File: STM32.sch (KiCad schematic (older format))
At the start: 35 parts, among them U1 STM32H753IIKx, U4 FM25V02A-GTR, U9 USB3300-EZK-TR, Y1 16MHz, Y2 32.768, Y3 24MHz

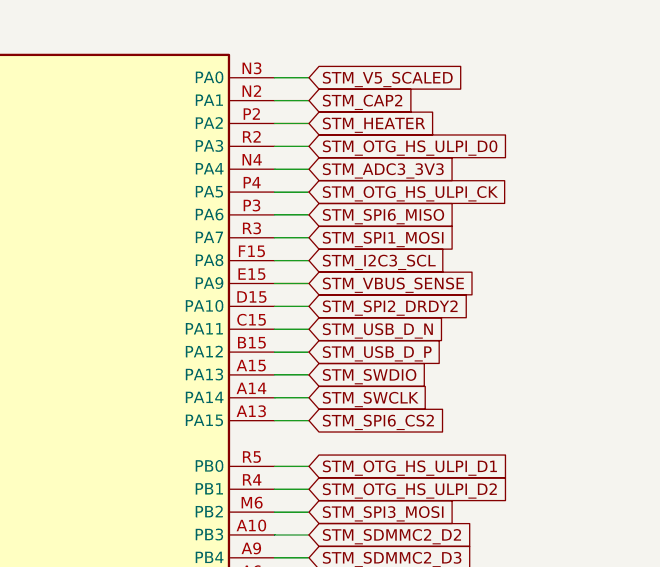
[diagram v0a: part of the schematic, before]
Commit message: start adding usb-c
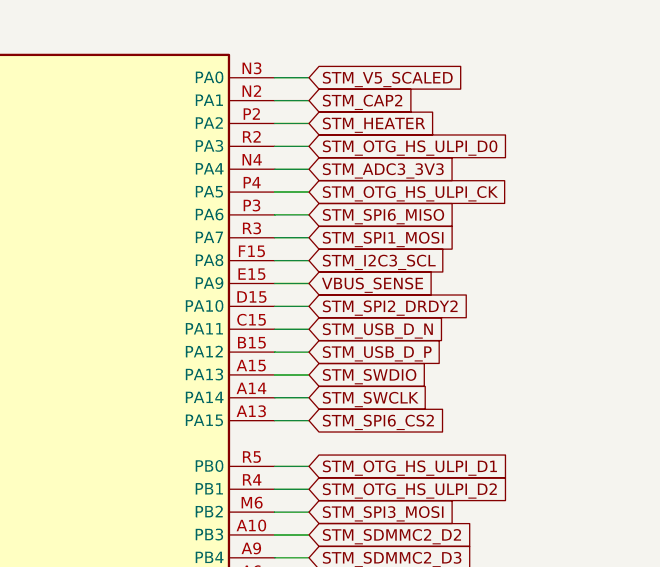
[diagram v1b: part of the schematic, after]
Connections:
- net STM_VBUS_SENSE: no longer U1.E15 (PA9)
- new net VBUS_SENSE: U1.E15 (PA9)
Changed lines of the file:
@@
 STM_SPI2_DRDY2
 Text GLabel 21450 2800 2    50   Input ~ 0
-STM_VBUS_SENSE
+VBUS_SENSE
 Text GLabel 21450 2700 2    50   Input ~ 0
 STM_I2C3_SCL

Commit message: working
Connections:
- net STM_VBUS_SENSE is gone; now on net VBUS_SENSE: U9.4 (VBUS)
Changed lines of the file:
@@
 Wire Wire Line
 	2650 9000 2650 8850
-Text GLabel 2950 8850 2    50   Input ~ 0
-SENSORS_3V3
 Wire Wire Line
 	2950 8850 2650 8850
@@
 Wire Wire Line
 	3400 5650 3400 5750
-Text GLabel 1550 4150 0    50   Input ~ 0
-STM_VBUS_SENSE
 Text GLabel 1550 4250 0    50   Input ~ 0
 USB_FMU_D_N
@@
 Wire Wire Line
 	900  4750 900  4650
+Text GLabel 1550 4150 0    50   Input ~ 0
+VBUS_SENSE
+Text GLabel 2950 8850 2    50   Input ~ 0
+SENSORS_3V3
 $EndSCHEMATC

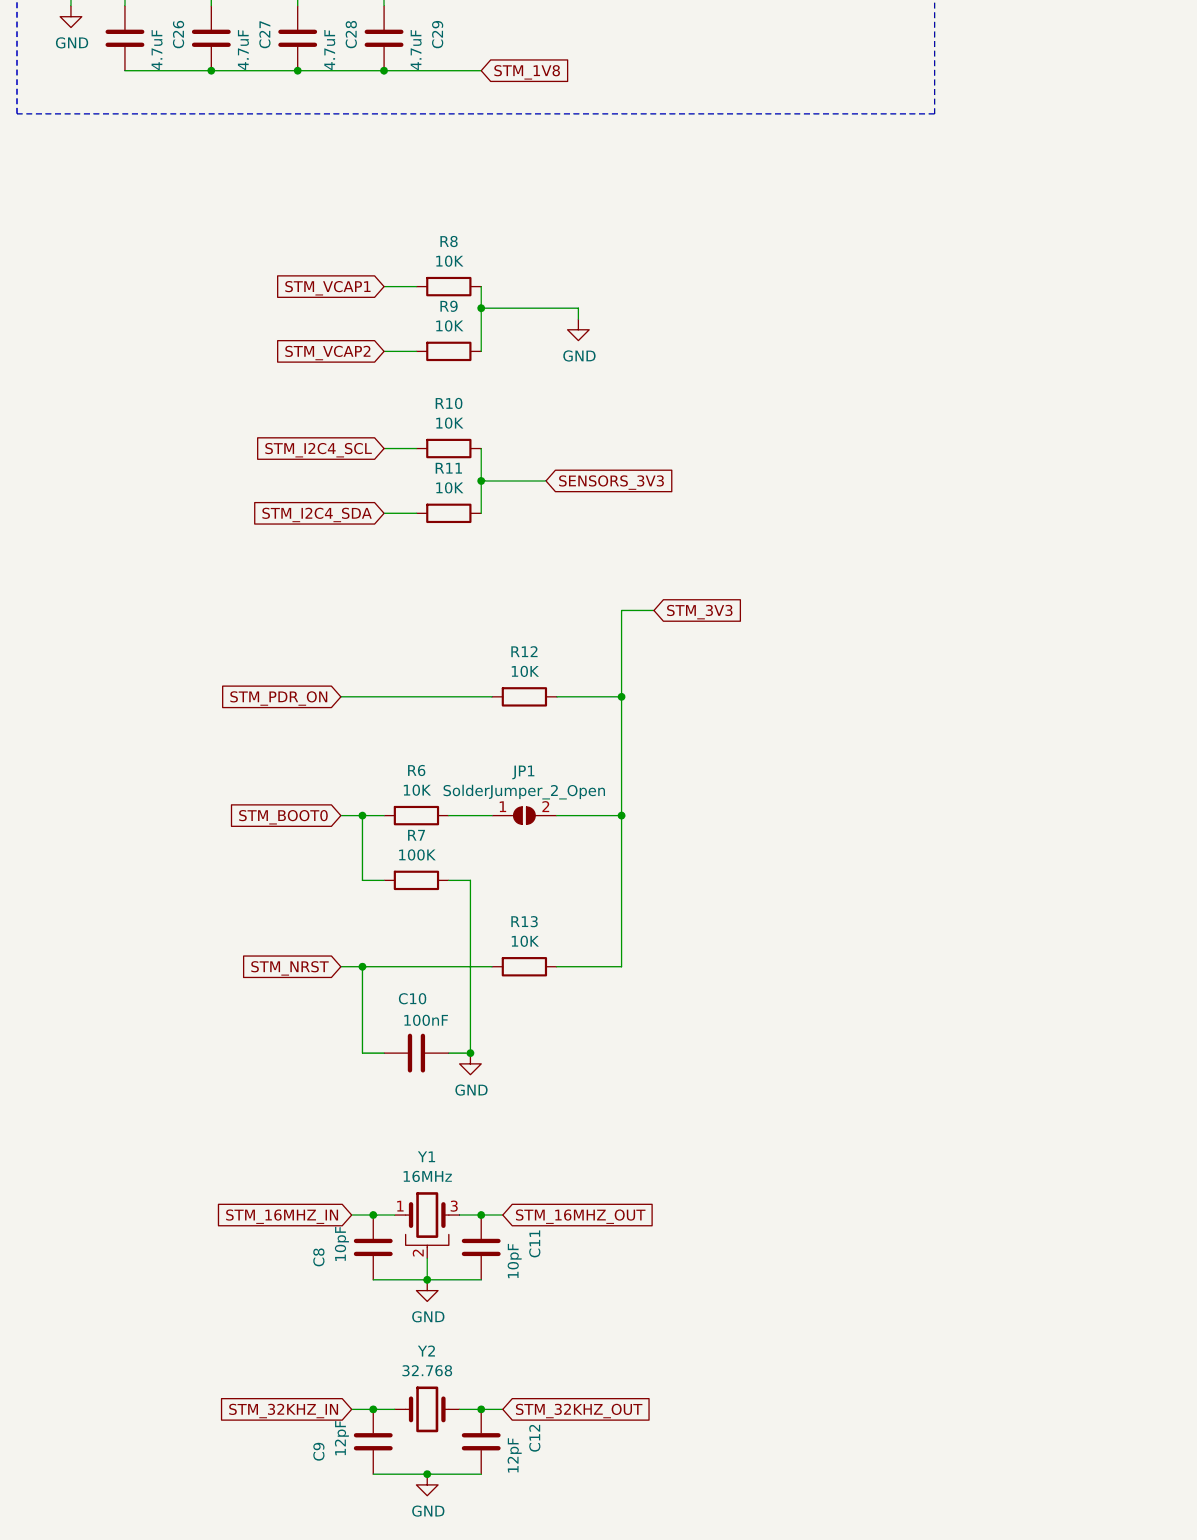
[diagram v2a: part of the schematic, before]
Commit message: start migrating to kicad v6
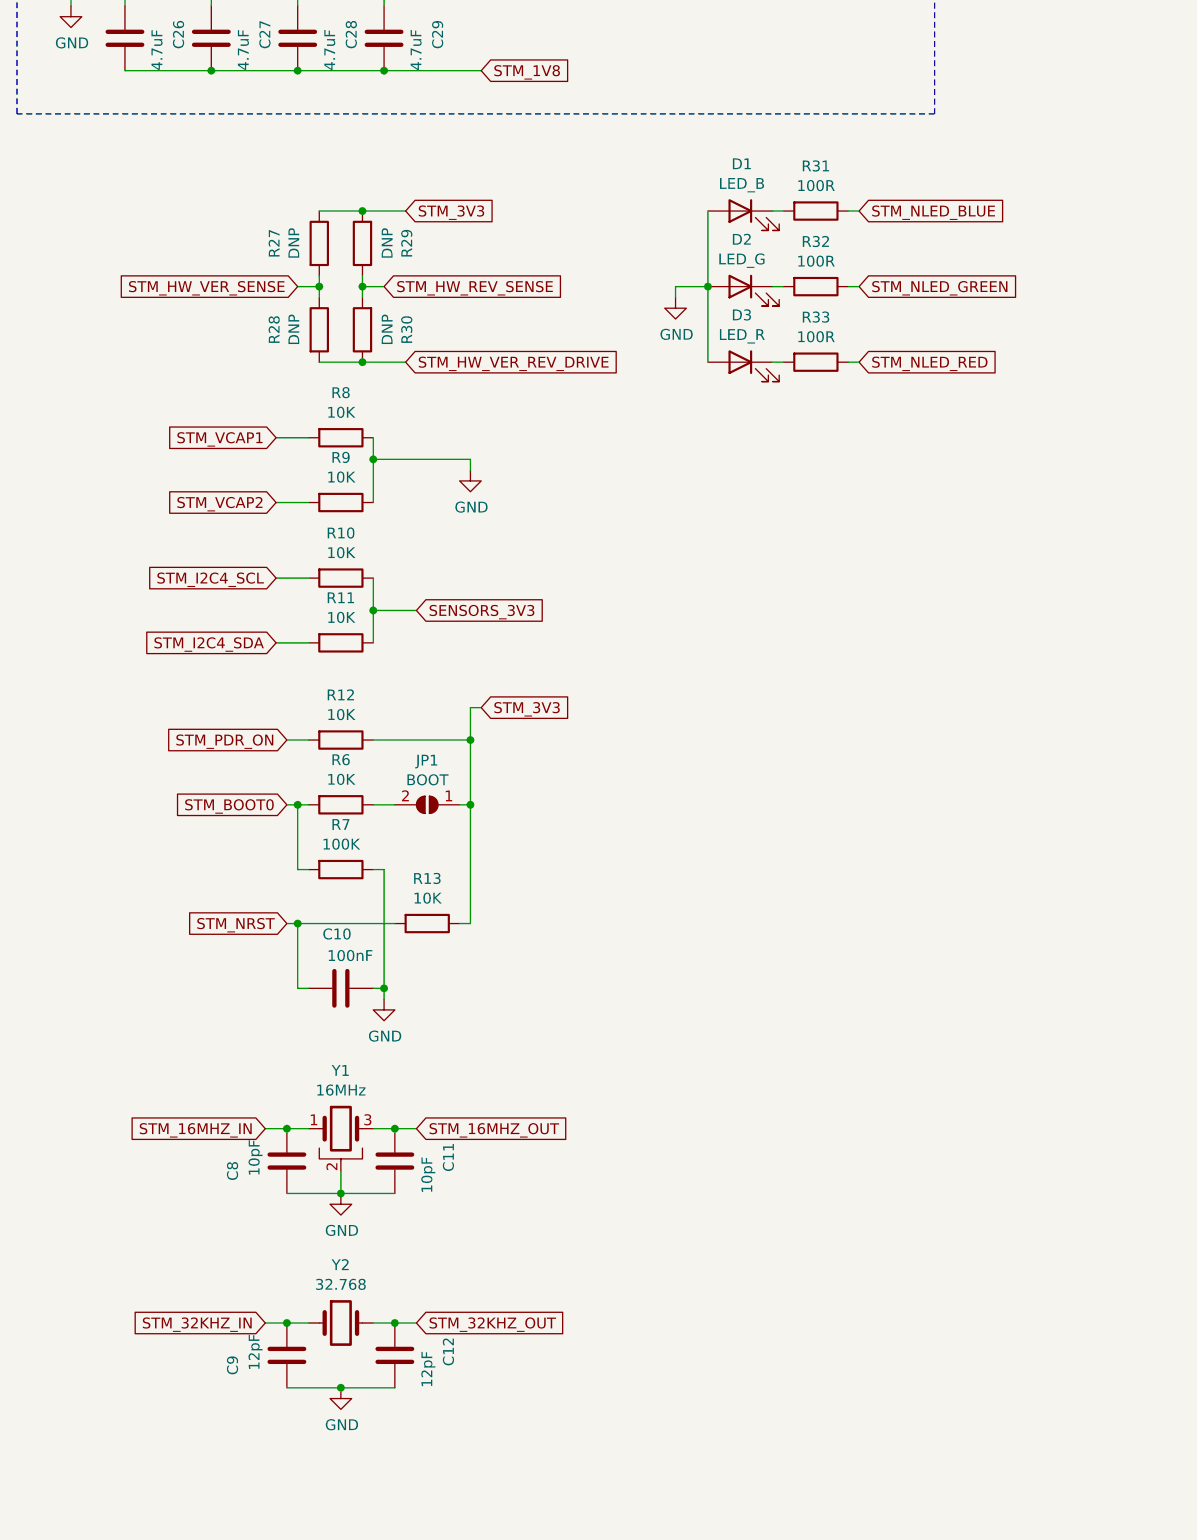
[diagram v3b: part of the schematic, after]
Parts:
- added D1: LED_B, symbol Device:LED
- added D2: LED_G, symbol Device:LED
- added D3: LED_R, symbol Device:LED
- added R27, R28, R29, R30: DNP, Resistor_SMD:R_0402_1005Metric, symbol Device:R
- added R31, R32, R33: 100R, Resistor_SMD:R_0402_1005Metric, symbol Device:R
- JP1: value SolderJumper_2_Open -> BOOT; Value SolderJumper_2_Open -> BOOT
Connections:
- net GND: now also D1.2 (A), D2.2 (A), D3.2 (A)
- net STM_3V3: now also JP1.1 (A), R27.1, R29.2; no longer JP1.2 (B)
- net STM_HW_REV_SENSE: now also R29.1, R30.2
- net STM_HW_VER_REV_DRIVE: now also R28.2, R30.1
- net STM_HW_VER_SENSE: now also R27.2, R28.1
- net STM_NLED_BLUE: now also R31.1
- net STM_NLED_GREEN: now also R32.1
- net STM_NLED_RED: now also R33.1
- net at R6.1: now also JP1.2 (B); no longer JP1.1 (A)
- new net: D1.1 (K), R31.2
- new net: D2.1 (K), R32.2
- new net: D3.1 (K), R33.2
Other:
- moved on the sheet: C10, C11, C12, C8, C9, JP1, R10, R11, R12, R13, R6, R7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
